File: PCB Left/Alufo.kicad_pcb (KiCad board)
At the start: 2 copper layers, 282.6 x 90.9 mm, 94 parts, among them J1 USB_C_Receptacle_USB2.0_16P_2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, J3 USB_C_Receptacle_USB2.0_16P_2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, K11 PG1350, K12 PG1350, K13 PG1350, K14 PG1350, K15 PG1350, K16 PG1350, K21 PG1350, K22 PG1350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

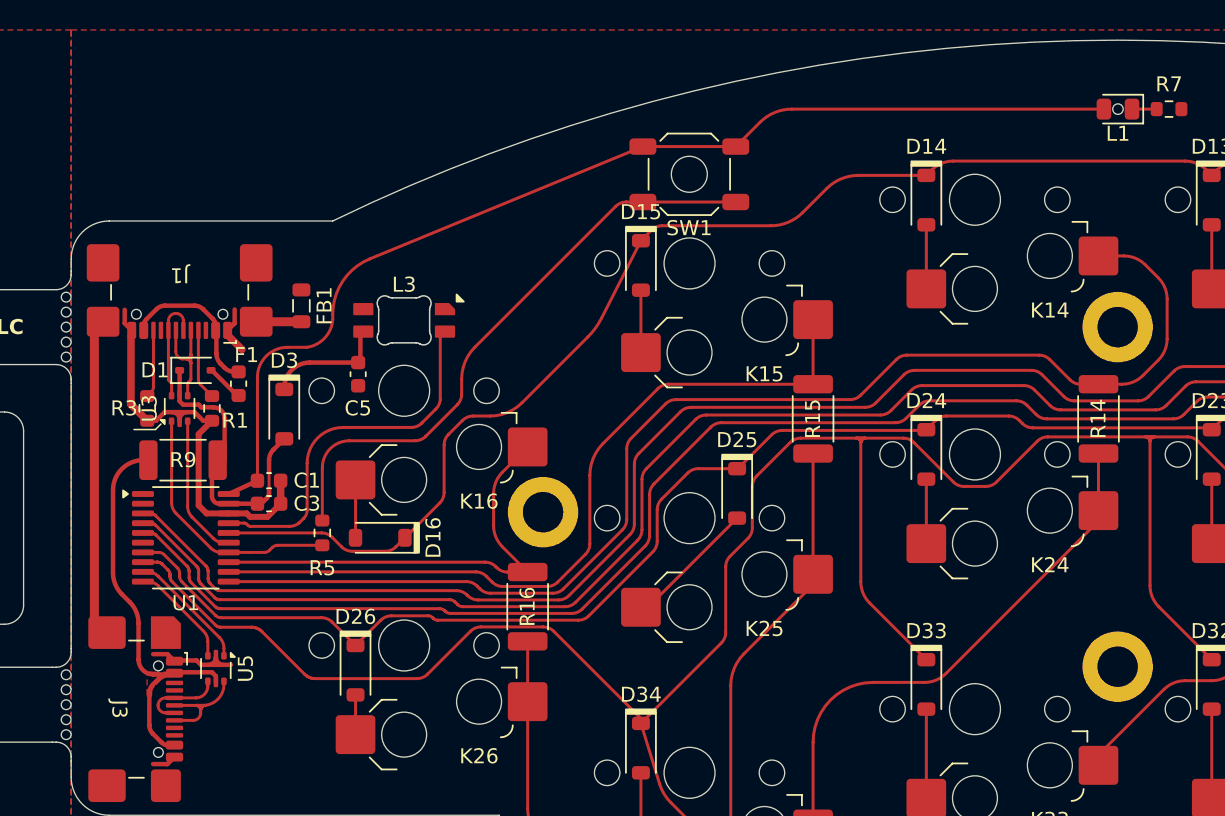
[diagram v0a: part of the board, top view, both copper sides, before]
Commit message: Remove 0Ω resistor (R9) on VCC line
Rework some routing around USB port.
Remove keep out areas from switch to allow additional ground connections.
Use personal SOD-323 footprint.
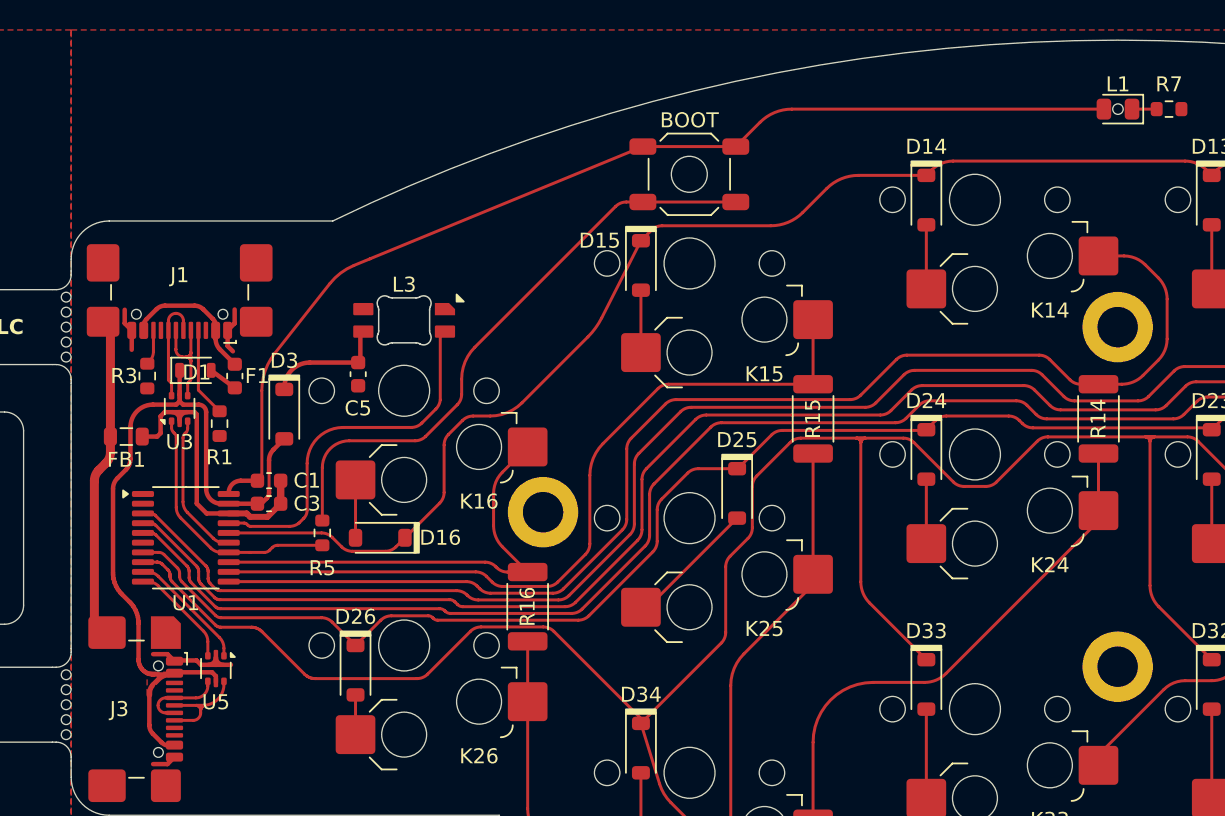
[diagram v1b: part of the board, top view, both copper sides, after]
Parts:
- removed NT1: NetTie_2, Project_Library:NetTie-2_SMD_Pad0.2mm
- removed R9: 0R, Resistor_SMD:R_2010_5025Metric
- D1: footprint Diode_SMD:D_SOD-323 -> BGK_Kicad:D_SOD-323
- moved FB1 14.6 mm to (172.0, 55.5), turned to 0 degrees
- moved R3 2.16 mm to (173.4, 51.4)
- moved R1 1.14 mm to (178.2, 54.6)
- moved F1 0.57 mm to (179.2, 51.4)
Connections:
- FB1 pad 1: Net-(FB1-Pad1) -> SHIELD
- J1 pad S2: Net-(FB1-Pad1) -> unconnected-(J1-SHIELD-PadS2)
- J3 pad A4: VCC' -> VCC
- J3 pad A9: VCC' -> VCC
- J3 pad B4: VCC' -> VCC
- J3 pad B9: VCC' -> VCC
- R5 pad 1: Net-(NT1-Pad2) -> USB+
- U5 pad 5: VCC' -> VCC
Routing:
- net VCC: track 18.8 -> 51.3 mm
- net VCC': track 27.7 -> 0.00 mm
- net USB+: track 11.2 -> 16.4 mm
- net Net-(NT1-Pad2): track 4.70 -> 0.00 mm
- net GND: track 32.2 -> 28.2 mm
- net Net-(FB1-Pad1): track 3.01 -> 0.00 mm
- net Net-(J1-CC2): track 3.79 -> 2.35 mm
- net Net-(J1-CC1): track 4.37 -> 5.62 mm
- net +3V3: track 72.4 -> 71.6 mm
- net USB_P-: track 5.48 -> 6.09 mm
- added copper zone on F.Cu, net VCC
- removed copper zone on F.Cu, net VCC'

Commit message: Add additional pads to USB ports for strength
Also apply tweaks from left PCB to right.
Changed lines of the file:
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@@
 		(tags "USB 2.0 C Type-C Receptacle SMD 16P 16C USB4110-GF-A")
 		(property "Reference" "J1"
-			(at 0 0 0)
+			(at 0 -1.27 0)
 			(unlocked yes)
 			(layer "F.SilkS")
@@
 			(layers "*.Cu" "*.Mask")
 		)
+		(pad "" smd roundrect
+			(at -1.798333 0.825 180)
+			(size 2.75 2.5)
+			(layers "F.Cu" "F.Mask" "F.Paste")
+			(roundrect_rratio 0.125)
+			(thermal_bridge_angle 45)
+		)
+		(pad "" smd roundrect
+			(at 1.798333 0.825 180)
+			(size 2.75 2.5)
+			(layers "F.Cu" "F.Mask" "F.Paste")
+			(roundrect_rratio 0.125)
+			(thermal_bridge_angle 45)
+		)
 		(pad "" np_thru_hole circle
 			(at 2.89 -2.605 180)
@@
 		(tags "USB 2.0 C Type-C Receptacle SMD 16P 16C USB4110-GF-A")
 		(property "Reference" "J3"
-			(at 0 0 0)
+			(at 0 -1.27 90)
 			(unlocked yes)
 			(layer "F.SilkS")
@@
 			(layers "*.Cu" "*.Mask")
 		)
+		(pad "" smd roundrect
+			(at -1.798333 0.825 270)
+			(size 2.75 2.5)
+			(layers "F.Cu" "F.Mask" "F.Paste")
+			(roundrect_rratio 0.125)
+			(thermal_bridge_angle 45)
+		)
+		(pad "" smd roundrect
+			(at 1.798333 0.825 270)
+			(size 2.75 2.5)
+			(layers "F.Cu" "F.Mask" "F.Paste")
+			(roundrect_rratio 0.125)
+			(thermal_bridge_angle 45)
+		)
 		(pad "" np_thru_hole circle
 			(at 2.89 -2.605 270)
@@
 			(layers "F.Cu" "F.Mask" "F.Paste")
 			(roundrect_rratio 0.125)
-			(chamfer_ratio 0.24)
-			(chamfer top_left)
 			(net 67 "unconnected-(J3-SHIELD-PadS2)")
 			(pinfunction "SHIELD")

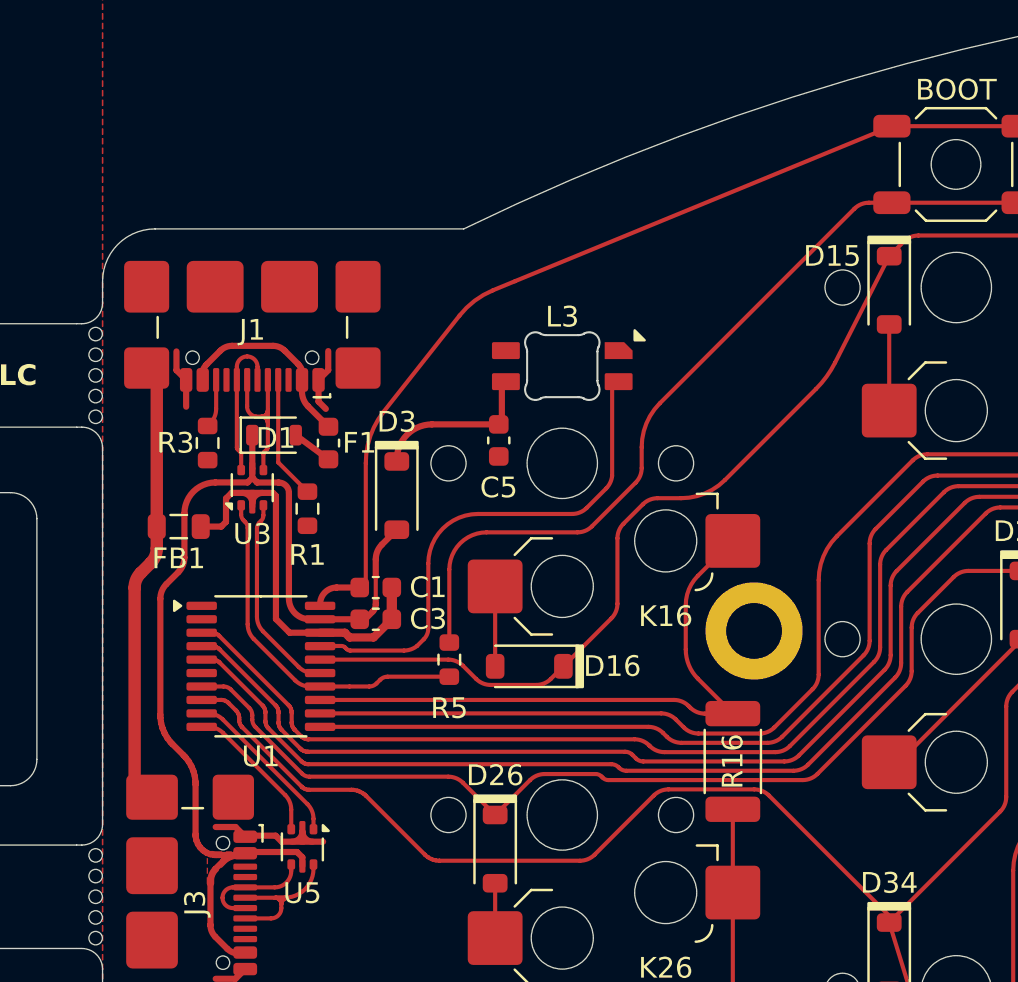
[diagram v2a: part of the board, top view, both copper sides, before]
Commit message: Move lefthand USB port in
Moved port and associated components 19.05÷12mm right to account for SMD legs.
Flipped fuse and Schottky to other side of USBLC6.
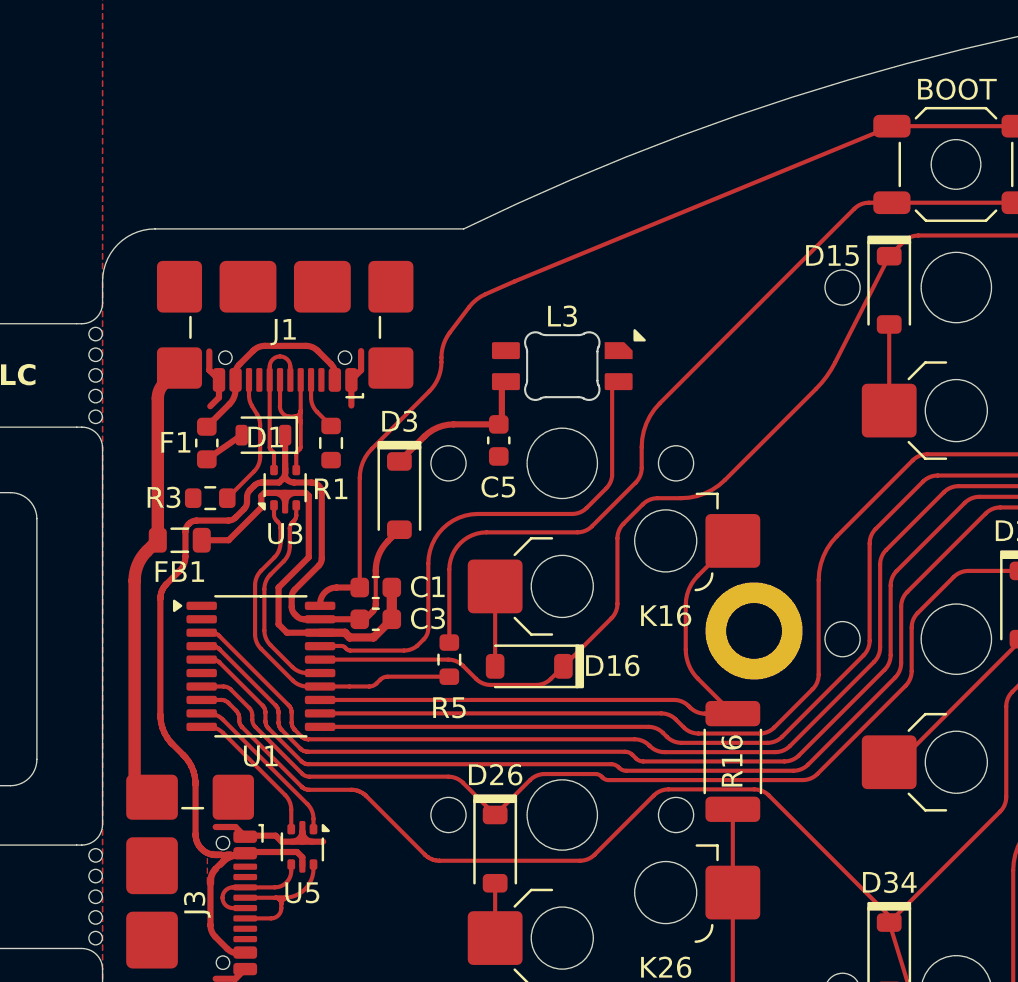
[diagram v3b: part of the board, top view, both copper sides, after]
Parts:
- moved F1 5.88 mm to (173.3, 51.4)
- moved R1 3.37 mm to (179.3, 51.4)
- moved R3 2.67 mm to (173.5, 54.1), turned to 180 degrees
- moved J1 1.59 mm to (177.1, 44.7)
- moved U3 1.59 mm to (177.1, 53.6)
- moved FB1 0.66 mm to (172.0, 56.1)
- moved D1 0.51 mm to (176.1, 51.1), turned to 180 degrees
- moved D3 0.13 mm to (182.6, 54.0)
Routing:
- net Net-(J1-CC2): track 2.35 -> 6.45 mm
- net Net-(J1-CC1): track 5.62 -> 2.58 mm
- net VCC: track 51.3 -> 53.5 mm
- net GND: track 28.2 -> 29.6 mm
- net USB+: track 16.4 -> 17.2 mm
- net USB-: track 9.48 -> 10.3 mm

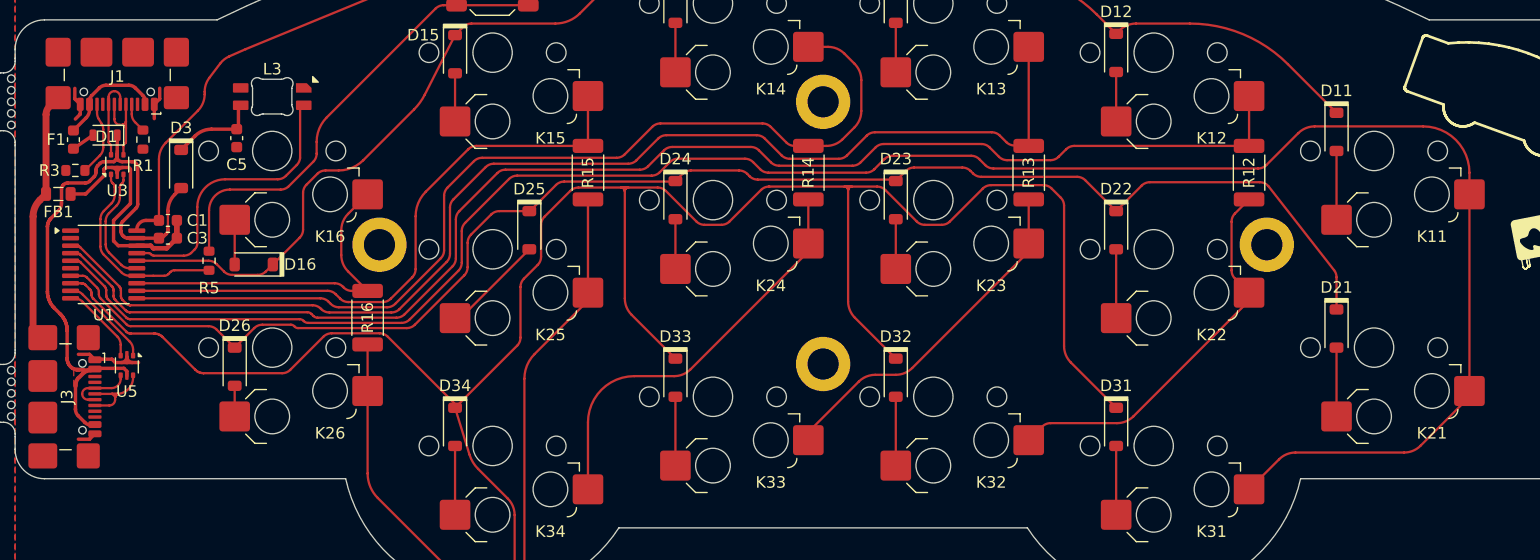
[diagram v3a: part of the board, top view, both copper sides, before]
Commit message: Remove lefthand R12
Can route Col1, Col2 and Row2 around each other without needing jumper on Col2.
Col1 and Col2 pins on MCU swapped.
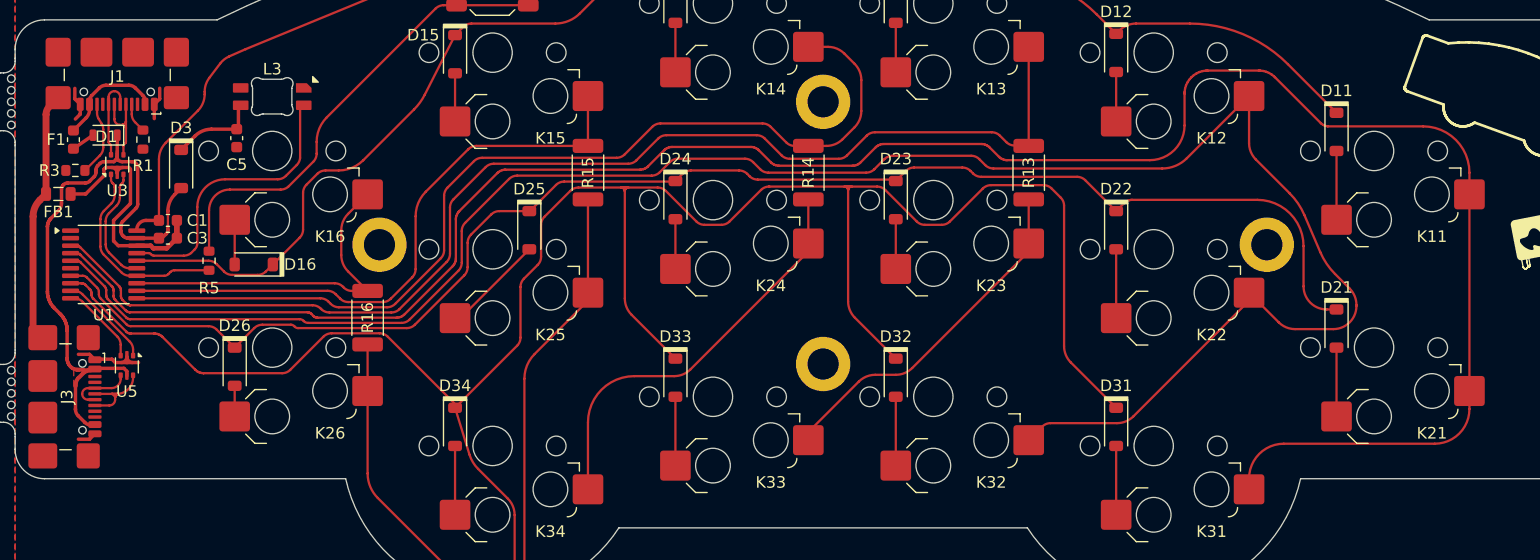
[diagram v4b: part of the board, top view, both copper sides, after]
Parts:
- removed R12: 0R, Resistor_SMD:R_2010_5025Metric
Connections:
- K22 pad 1: Net-(K22-Pad1) -> Col2
- K32 pad 1: Net-(K22-Pad1) -> Col2
- U1 pad 4: Col2 -> Col1
- U1 pad 5: Col1 -> Col2
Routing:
- net Col2: track 118.8 -> 172.0 mm
- net Net-(K22-Pad1): track 33.1 -> 0.00 mm
- net Col1: track 176.4 -> 185.3 mm
- net VCC: track 53.5 -> 52.2 mm
- net Row2: track 130.2 -> 129.3 mm
- net USB-: track 10.3 -> 9.62 mm
- net USB+: track 17.2 -> 16.6 mm

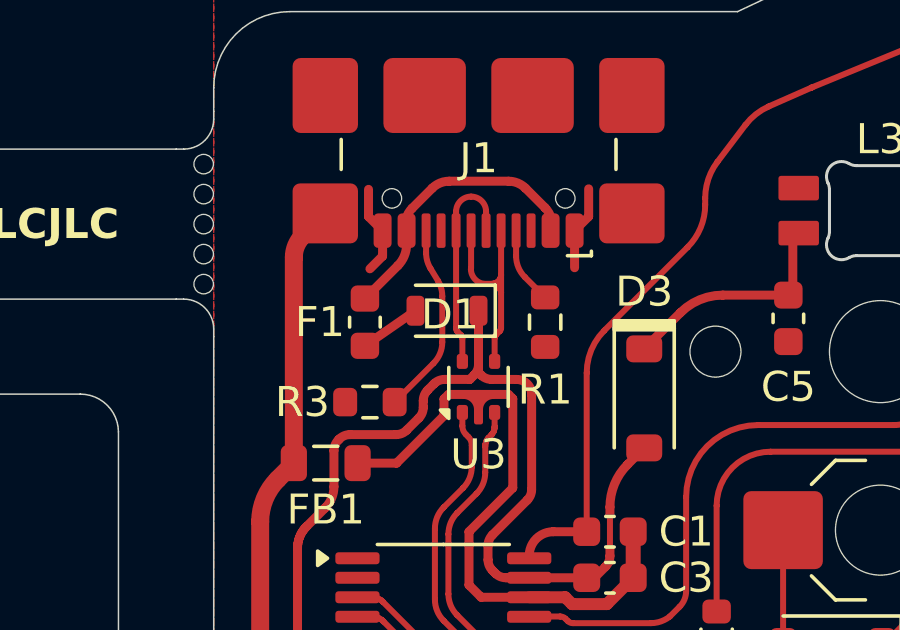
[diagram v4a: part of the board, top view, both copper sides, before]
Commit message: Update LCSC part number for USB ports
Also hide LCSC numbers erroneously showing in schematic.
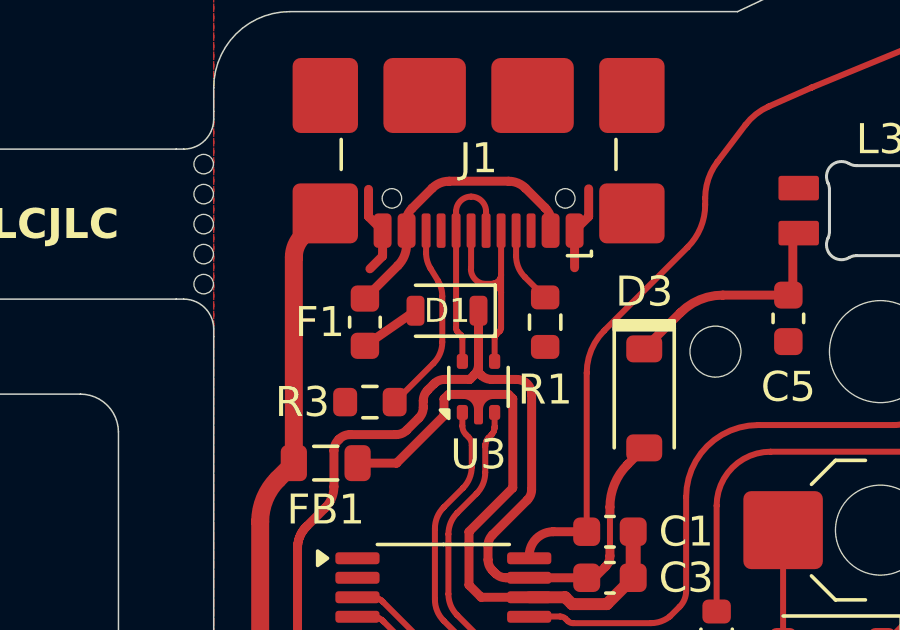
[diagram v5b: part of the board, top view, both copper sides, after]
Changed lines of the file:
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@@
 			)
 		)
-		(property "LCSC" "C5143397"
+		(property "LCSC" "C2681552"
 			(at 0 0 180)
 			(unlocked yes)
@@
 			)
 		)
-		(property "LCSC" "C5143397"
+		(property "LCSC" "C2681552"
 			(at 0 0 270)
 			(unlocked yes)
@@
 		(tags "SOD-323")
 		(property "Reference" "D1"
-			(at -0.1 -0.127 0)
+			(at 0 0 0)
 			(layer "F.SilkS")
 			(effects
 				(font
-					(size 1 1)
-					(thickness 0.15)
+					(size 0.8 0.8)
+					(thickness 0.12)
 				)
 			)

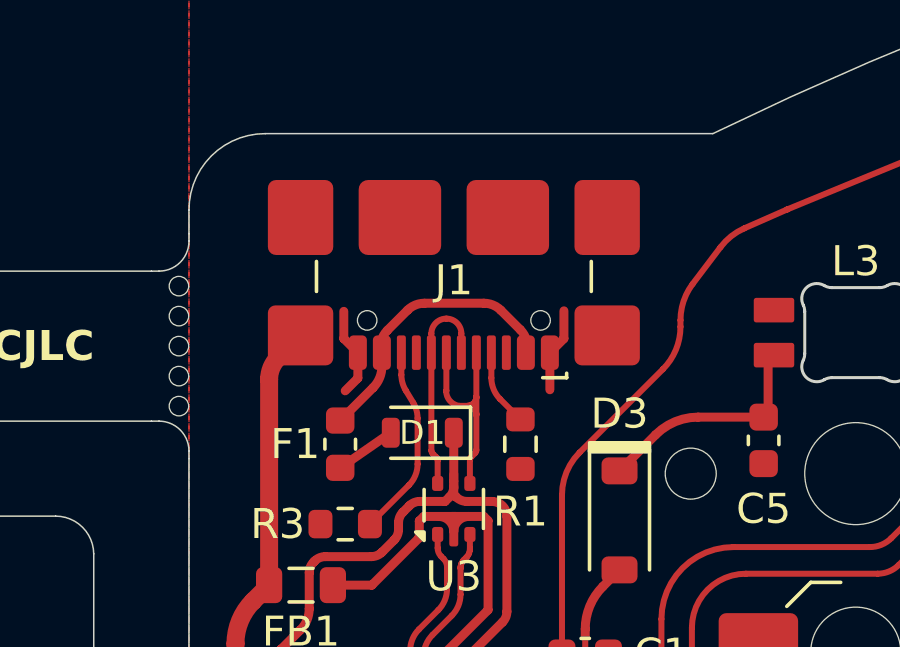
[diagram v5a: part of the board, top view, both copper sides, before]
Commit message: Fix PCB edge marker on USB port
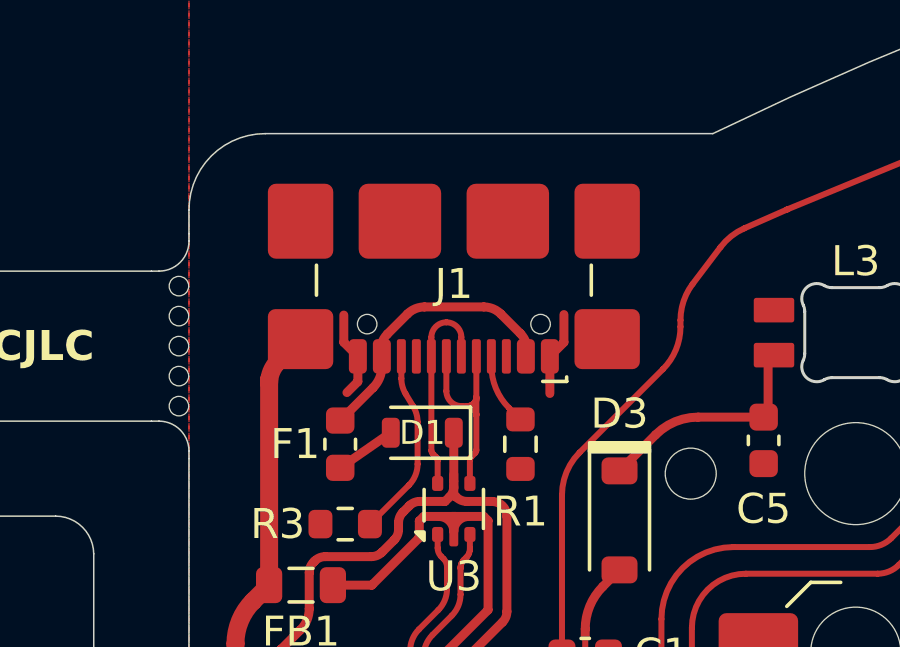
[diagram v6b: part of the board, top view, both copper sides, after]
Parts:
- moved J1 0.12 mm to (177.1, 44.8)
